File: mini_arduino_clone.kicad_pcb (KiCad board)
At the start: 4 copper layers, 45.1 x 18 mm, 31 parts, among them J101 USB_B_Micro, J102 Conn_02x03_Odd_Even, J103 Conn_01x13, J104 Conn_01x13, SW101 SW_Push, U101 ATmega328P-AU, U201 XC6220B331MR-G, U301 CP2102-GMR, Y101 16MHz

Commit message: update parts
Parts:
- added G***: LOGO, User_Footprint:arduino-logo-10x20mm, B.Cu at (98.6, 57.9)
- D1: value MSS1P4 -> B5819W; footprint Diode_SMD:D_MicroSMP_AK -> Diode_SMD:D_SOD-123
- moved C102 0.89 mm to (71.6, 63.4)
- moved U201 0.53 mm to (85.2, 62.2)
- moved D1 0.38 mm to (80.8, 63.2)
- moved C202 0.28 mm to (88.0, 62.1)
- moved F101 0.25 mm to (76.1, 63.0)
- moved C201 0.08 mm to (80.1, 61.3)
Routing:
- net GND: track 40.7 -> 40.0 mm
- net +5V: track 23.2 -> 22.6 mm
- net +3V3: track 19.1 -> 19.7 mm
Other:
- board text added: "3V3"
- board text added: "5V"
- board text added: "A0"
- board text added: "A1"
- board text added: "A2"
- board text added: "A3"
- board text added: "A4"
- board text added: "A5"
- board text added: "A6"
- board text added: "A7"
- board text added: "Arduino Nano Clone Butler's Lab/Rev. ${REVISION} ${ISSUE_DATE}"
- board text added: "D10"
- board text added: "D11"
- board text added: "D12"
- board text added: "D13"
- board text added: "D2"
- board text added: "D3"
- board text added: "D4"
- board text added: "D5"
- board text added: "D6"
- board text added: "D7"
- board text added: "D8"
- board text added: "D9"
- board text added: "G"
- board text added: "RST"
- board text added: "RX"
- board text added: "TX"
- board text added: "VBUS"

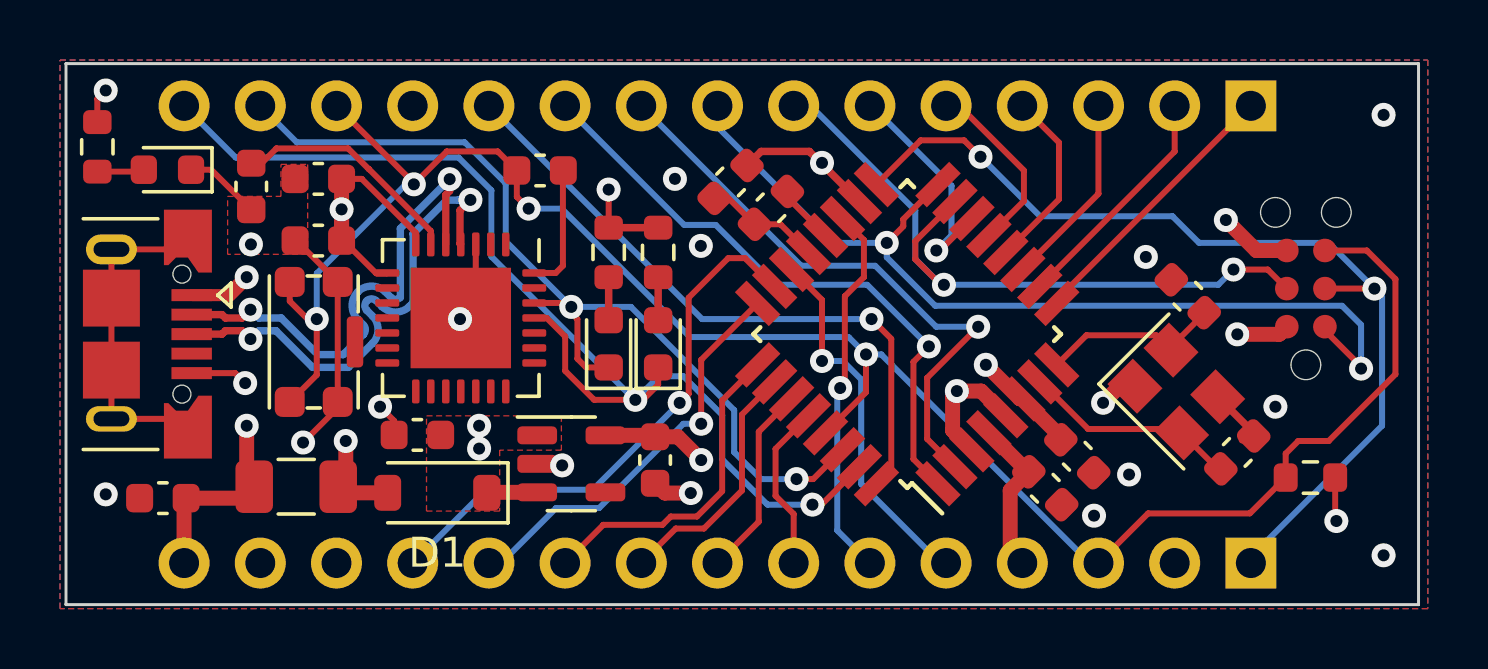
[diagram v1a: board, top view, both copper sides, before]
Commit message: fix pin assignments on crystal
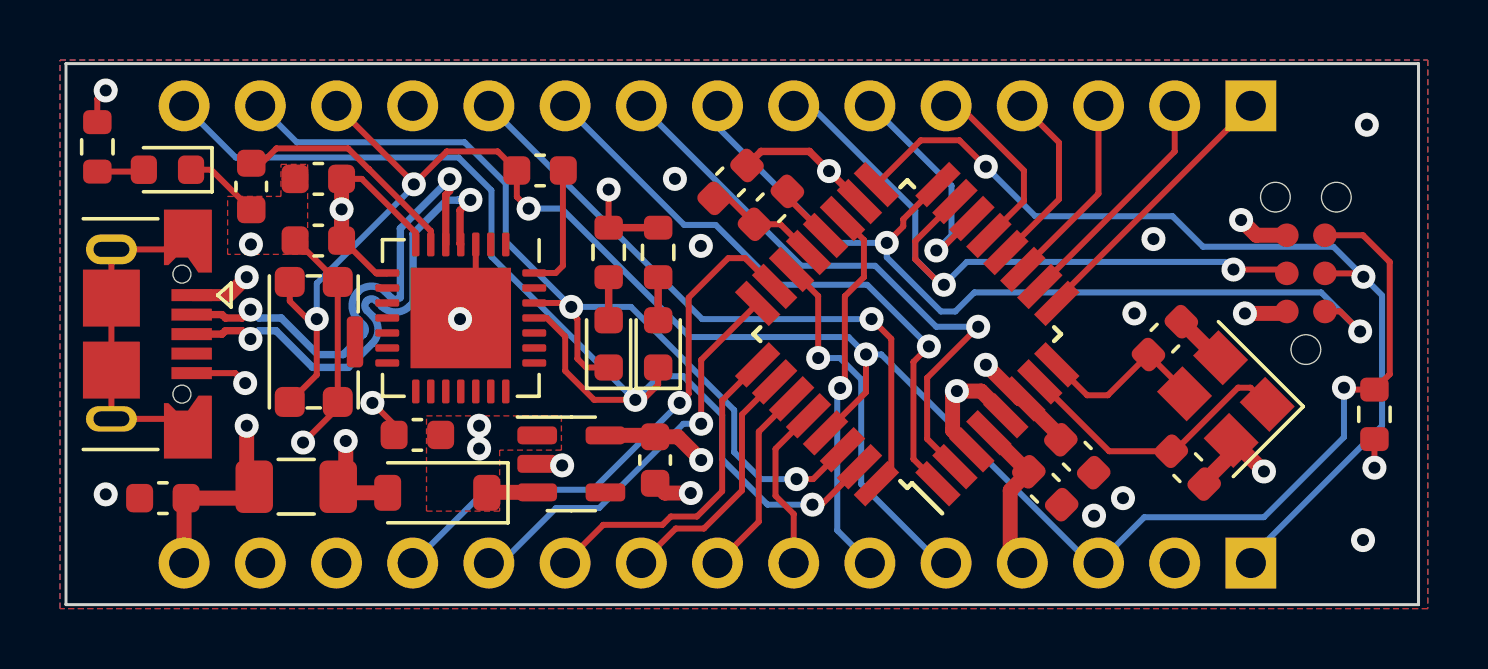
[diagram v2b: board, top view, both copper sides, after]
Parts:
- moved R103 3.00 mm to (112.0, 60.6), turned to 90 degrees
- moved C105 1.73 mm to (105.8, 62.4), turned to -45 degrees
- moved Y101 1.67 mm to (107.1, 60.1), turned to 135 degrees
- moved C107 1.59 mm to (105.0, 58.0), turned to 45 degrees
- moved J102 0.51 mm to (109.7, 55.9)
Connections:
- Y101 pad 1: GND -> /XTAL1
- Y101 pad 2: /XTAL1 -> GND
- Y101 pad 3: GND -> /XTAL2
- Y101 pad 4: /XTAL2 -> GND
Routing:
- net /XTAL1: track 7.06 -> 9.65 mm
- net GND: track 40.0 -> 41.6 mm
- net /D12/MISO: track 31.2 -> 29.9 mm
- net +5V: track 22.6 -> 21.7 mm
- net /~{RESET}: track 66.1 -> 66.7 mm, vias 4 -> 5

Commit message: update production files
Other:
- board text added: "JLCJLCJLCJLC"
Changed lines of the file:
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@@
   (title_block
     (title "Arduino Nano Clone")
-    (date "2023-06-02")
+    (date "2023-06-05")
     (rev "B")
     (company "Butler's Lab")
@@
     (effects (font (size 1 0.7) (thickness 0.153)) (justify mirror))
   )
+  (gr_text "JLCJLCJLCJLC" (at 111.887 57.15 270) (layer "B.SilkS")
+    (effects (font (size 1 0.7) (thickness 0.153) bold) (justify bottom mirror))
+  )
   (gr_text "D4" (at 87.575107 52.3748) (layer "B.SilkS")
